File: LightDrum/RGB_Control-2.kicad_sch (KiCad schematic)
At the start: 25 parts, among them Q401 PMXB43UNEZ, Q402 PMXB43UNEZ, Q403 PMXB43UNEZ, Q404 PMXB43UNEZ, Q405 PMXB43UNEZ, Q406 PMXB43UNEZ, Q407 PMXB43UNEZ, Q408 PMXB43UNEZ, U401 PCA9634_TSSOP20

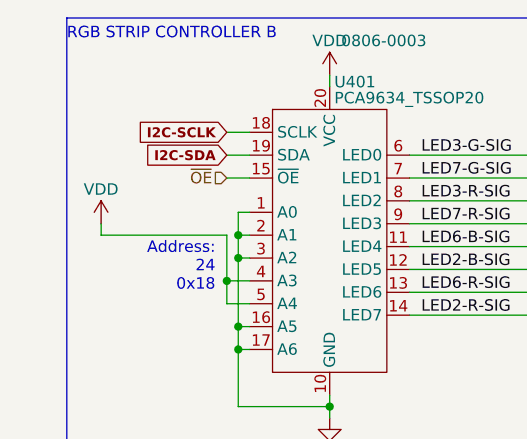
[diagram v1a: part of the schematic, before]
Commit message: Preliminary schematic lock - Starting PCB layout
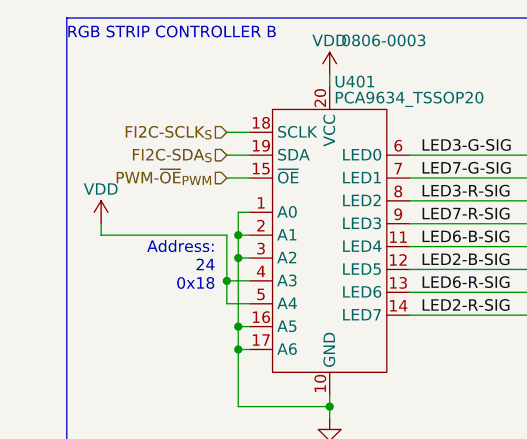
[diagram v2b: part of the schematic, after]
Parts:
- Q401, Q402, Q403, Q404, Q405, Q406, Q407, Q408: SupplierPN (none) -> 1727-PMXB43UNEZCT-ND
- R401, R402, R403, R404, R409, R410, R411, R412: SupplierPN (none) -> RMCF0402FT100RCT-ND
- R405, R406, R407, R408, R413, R414, R415, R416: SupplierPN (none) -> 311-10KJRCT-ND
- U401: SupplierPN (none) -> 568-4066-1-ND
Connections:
- net I2C-SCLK renamed FI2C-SCLK_{S}
- net I2C-SDA renamed FI2C-SDA_{S}
- net ~{OE} renamed PWM-~{OE}_{PWM}
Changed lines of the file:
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@@
   (title_block
     (title "LightDrum")
-    (rev "REV10")
+    (rev "REV11")
     (company "Daxxn Industries")
   )
@@
     (effects (font (size 1.27 1.27)) (justify left bottom))
   )
-  (global_label "I2C-SCLK" (shape input) (at 34.29 29.21 180) (fields_autoplaced)
-    (effects (font (size 1.1 1.1) (thickness 0.254) bold) (justify right))
-    (property "Intersheetrefs" "${INTERSHEET_REFS}" (at 23.7956 29.083 0)
-      (effects (font (size 1.1 1.1) (thickness 0.254) bold) (justify right) hide)
-    )
-  )
-  (global_label "I2C-SDA" (shape input) (at 34.29 31.75 180) (fields_autoplaced)
-    (effects (font (size 1.1 1.1) (thickness 0.254) bold) (justify right))
-    (property "Intersheetrefs" "${INTERSHEET_REFS}" (at 24.8432 31.623 0)
-      (effects (font (size 1.1 1.1) (thickness 0.254) bold) (justify right) hide)
-    )
-  )
   (hierarchical_label "LED6-B" (shape output) (at 102.87 44.45 0) (fields_autoplaced)
     (effects (font (size 1.27 1.27)) (justify left))
   )
-  (hierarchical_label "~{OE}" (shape input) (at 34.29 34.29 180) (fields_autoplaced)
+  (hierarchical_label "FI2C-SCLK_{S}" (shape input) (at 34.29 29.21 180) (fields_autoplaced)
+    (effects (font (size 1.27 1.27)) (justify right))
+  )
+  (hierarchical_label "PWM-~{OE}_{PWM}" (shape input) (at 34.29 34.29 180) (fields_autoplaced)
     (effects (font (size 1.27 1.27)) (justify right))
   )
@@
   (hierarchical_label "LED7-R" (shape output) (at 115.57 68.58 0) (fields_autoplaced)
     (effects (font (size 1.27 1.27)) (justify left))
+  )
+  (hierarchical_label "FI2C-SDA_{S}" (shape input) (at 34.29 31.75 180) (fields_autoplaced)
+    (effects (font (size 1.27 1.27)) (justify right))
   )
   (hierarchical_label "LED7-G" (shape output) (at 166.37 68.58 0) (fields_autoplaced)
@@
       (effects (font (size 1.27 1.27)) hide)
     )
+    (property "SupplierPN" "311-10KJRCT-ND" (at 172.72 53.34 0)
+      (effects (font (size 1.27 1.27)) hide)
+    )
     (pin "1")
     (pin "2")
@@
       (effects (font (size 1.27 1.27)) (justify left))
     )
+    (property "SupplierPN" "1727-PMXB43UNEZCT-ND" (at 163.83 73.66 0)
+      (effects (font (size 1.27 1.27)) hide)
+    )
     (pin "1")
     (pin "2")
@@
     (property "PartNumber" "0806-0003" (at 46.99 19.05 0)
       (effects (font (size 1.27 1.27)) (justify left))
+    )
+    (property "SupplierPN" "568-4066-1-ND" (at 45.72 40.64 0)
+      (effects (font (size 1.27 1.27)) hide)
     )
     (pin "1")
@@
       (effects (font (size 1.27 1.27)) hide)
     )
+    (property "SupplierPN" "311-10KJRCT-ND" (at 185.42 77.47 0)
+      (effects (font (size 1.27 1.27)) hide)
+    )
     (pin "1")
     (pin "2")
@@
       (effects (font (size 1.27 1.27)) hide)
     )
+    (property "SupplierPN" "RMCF0402FT100RCT-ND" (at 172.72 45.72 0)
+      (effects (font (size 1.27 1.27)) hide)
+    )
     (pin "1")
     (pin "2")
@@
       (effects (font (size 1.27 1.27)) hide)
     )
+    (property "SupplierPN" "RMCF0402FT100RCT-ND" (at 160.02 69.85 0)
+      (effects (font (size 1.27 1.27)) hide)
+    )
     (pin "1")
     (pin "2")
@@
       (effects (font (size 1.27 1.27)) hide)
     )
+    (property "SupplierPN" "311-10KJRCT-ND" (at 109.22 77.47 0)
+      (effects (font (size 1.27 1.27)) hide)
+    )
     (pin "1")
     (pin "2")
@@
       (effects (font (size 1.27 1.27)) (justify left))
     )
+    (property "SupplierPN" "1727-PMXB43UNEZCT-ND" (at 100.33 49.53 0)
+      (effects (font (size 1.27 1.27)) hide)
+    )
     (pin "1")
     (pin "2")
@@
       (effects (font (size 1.27 1.27)) (justify left))
     )
+    (property "SupplierPN" "1727-PMXB43UNEZCT-ND" (at 151.13 49.53 0)
+      (effects (font (size 1.27 1.27)) hide)
+    )
     (pin "1")
     (pin "2")
@@
       (effects (font (size 1.27 1.27)) hide)
     )
+    (property "SupplierPN" "RMCF0402FT100RCT-ND" (at 147.32 45.72 0)
+      (effects (font (size 1.27 1.27)) hide)
+    )
     (pin "1")
     (pin "2")
@@
       (effects (font (size 1.27 1.27)) hide)
     )
+    (property "SupplierPN" "RMCF0402FT100RCT-ND" (at 134.62 69.85 0)
+      (effects (font (size 1.27 1.27)) hide)
+    )
     (pin "1")
     (pin "2")
@@
       (effects (font (size 1.27 1.27)) (justify left))
     )
+    (property "SupplierPN" "1727-PMXB43UNEZCT-ND" (at 113.03 73.66 0)
+      (effects (font (size 1.27 1.27)) hide)
+    )
     (pin "1")
     (pin "2")
@@
     (property "PartNumber" "0703-0003" (at 128.27 45.72 0)
       (effects (font (size 1.27 1.27)) (justify left))
+    )
+    (property "SupplierPN" "1727-PMXB43UNEZCT-ND" (at 125.73 49.53 0)
+      (effects (font (size 1.27 1.27)) hide)
     )
     (pin "1")
@@
       (effects (font (size 1.27 1.27)) hide)
     )
+    (property "SupplierPN" "RMCF0402FT100RCT-ND" (at 121.92 45.72 0)
+      (effects (font (size 1.27 1.27)) hide)
+    )
     (pin "1")
     (pin "2")
@@
       (effects (font (size 1.27 1.27)) hide)
     )
+    (property "SupplierPN" "311-10KJRCT-ND" (at 147.32 53.34 0)
+      (effects (font (size 1.27 1.27)) hide)
+    )
     (pin "1")
     (pin "2")
@@
       (effects (font (size 1.27 1.27)) hide)
     )
+    (property "SupplierPN" "311-10KJRCT-ND" (at 134.62 77.47 0)
+      (effects (font (size 1.27 1.27)) hide)
+    )
     (pin "1")
     (pin "2")
@@
       (effects (font (size 1.27 1.27)) hide)
     )
+    (property "SupplierPN" "RMCF0402FT100RCT-ND" (at 96.52 45.72 0)
+      (effects (font (size 1.27 1.27)) hide)
+    )
     (pin "1")
     (pin "2")
@@
       (effects (font (size 1.27 1.27)) hide)
     )
+    (property "SupplierPN" "RMCF0402FT100RCT-ND" (at 109.22 69.85 0)
+      (effects (font (size 1.27 1.27)) hide)
+    )
     (pin "1")
     (pin "2")
@@
       (effects (font (size 1.27 1.27)) hide)
     )
+    (property "SupplierPN" "311-10KJRCT-ND" (at 160.02 77.47 0)
+      (effects (font (size 1.27 1.27)) hide)
+    )
     (pin "1")
     (pin "2")
@@
       (effects (font (size 1.27 1.27)) (justify left))
     )
+    (property "SupplierPN" "1727-PMXB43UNEZCT-ND" (at 138.43 73.66 0)
+      (effects (font (size 1.27 1.27)) hide)
+    )
     (pin "1")
     (pin "2")
@@
       (effects (font (size 1.27 1.27)) hide)
     )
+    (property "SupplierPN" "311-10KJRCT-ND" (at 121.92 53.34 0)
+      (effects (font (size 1.27 1.27)) hide)
+    )
     (pin "1")
     (pin "2")
@@
       (effects (font (size 1.27 1.27)) hide)
     )
+    (property "SupplierPN" "RMCF0402FT100RCT-ND" (at 185.42 69.85 0)
+      (effects (font (size 1.27 1.27)) hide)
+    )
     (pin "1")
     (pin "2")
@@
       (effects (font (size 1.27 1.27)) (justify left))
     )
+    (property "SupplierPN" "1727-PMXB43UNEZCT-ND" (at 176.53 49.53 0)
+      (effects (font (size 1.27 1.27)) hide)
+    )
     (pin "1")
     (pin "2")
@@
       (effects (font (size 1.27 1.27)) (justify left))
     )
+    (property "SupplierPN" "1727-PMXB43UNEZCT-ND" (at 189.23 73.66 0)
+      (effects (font (size 1.27 1.27)) hide)
+    )
     (pin "1")
     (pin "2")
@@
       (effects (font (size 1.27 1.27)) hide)
     )
+    (property "SupplierPN" "311-10KJRCT-ND" (at 96.52 53.34 0)
+      (effects (font (size 1.27 1.27)) hide)
+    )

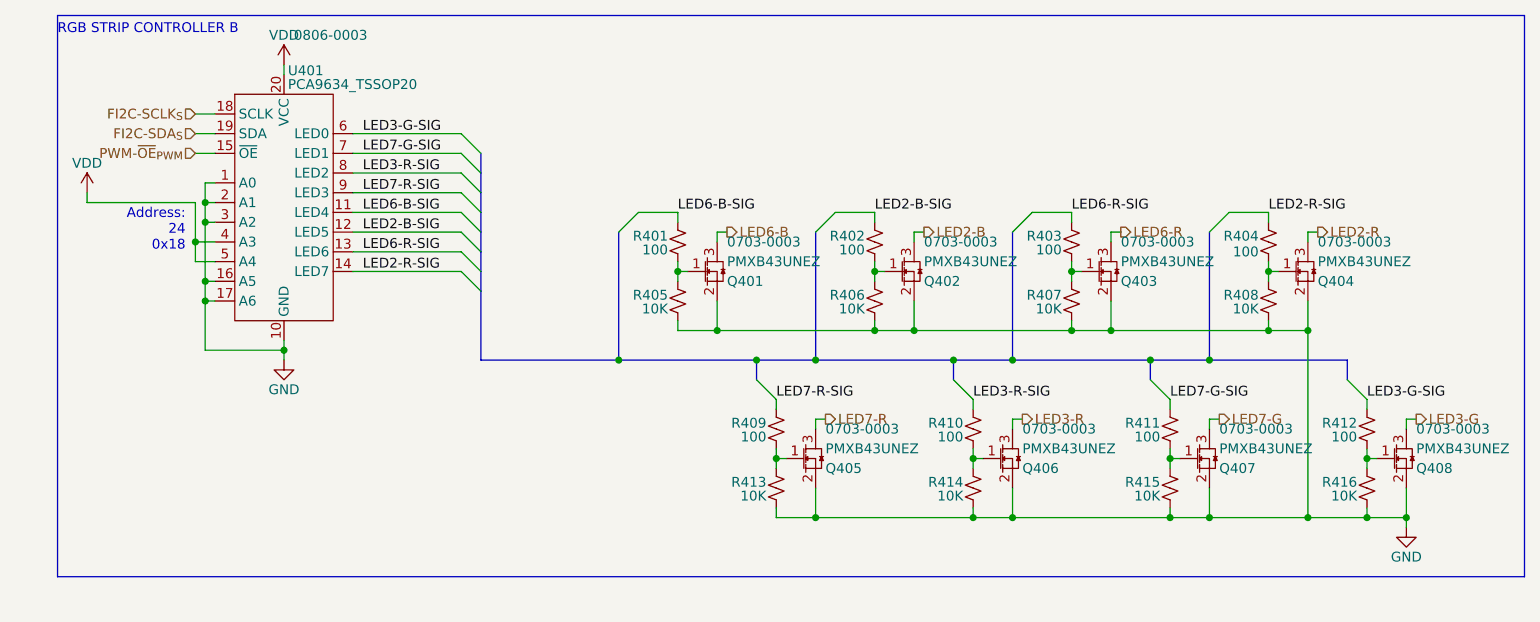
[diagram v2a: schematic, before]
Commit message: Component placement complete
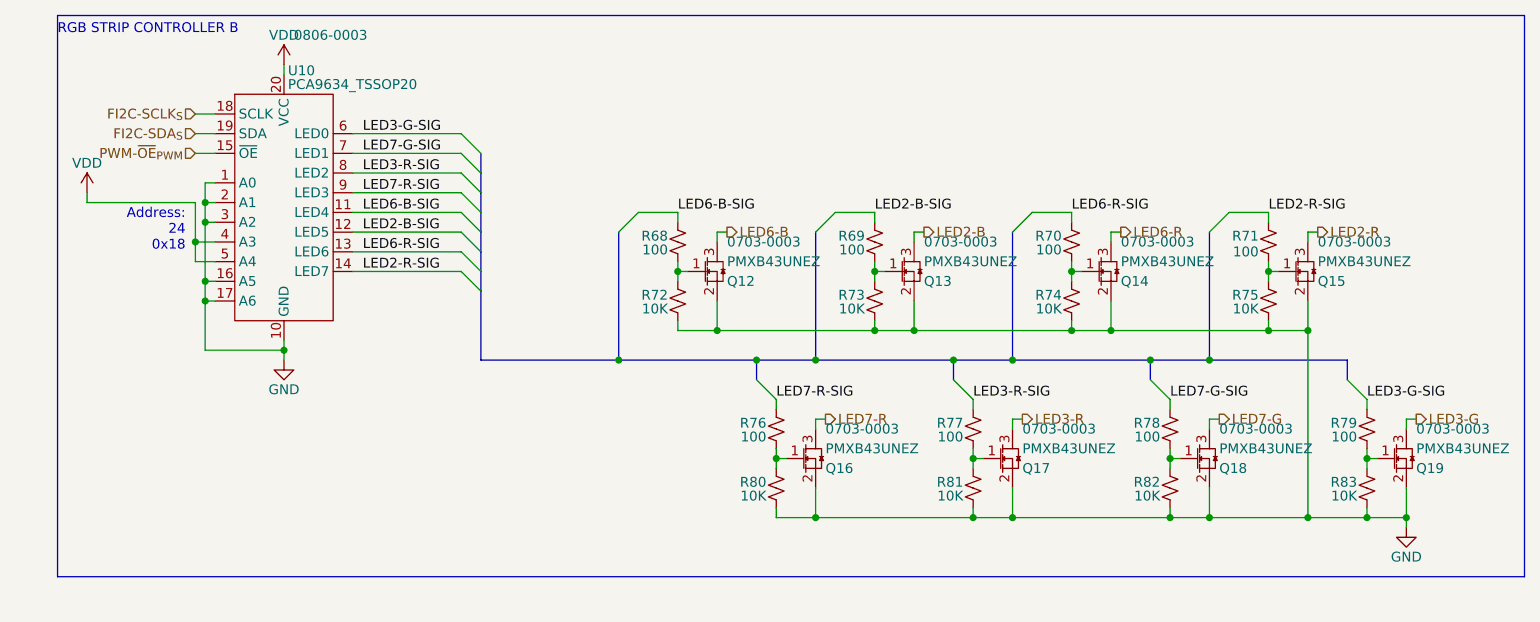
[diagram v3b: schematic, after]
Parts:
- renumbered Q401 to Q12, Q402 to Q13, Q403 to Q14, Q404 to Q15, Q405 to Q16, Q406 to Q17, Q407 to Q18, Q408 to Q19, R401 to R68, R402 to R69, R403 to R70, R404 to R71, R405 to R72, R406 to R73, R407 to R74, R408 to R75, R409 to R76, R410 to R77, R411 to R78, R412 to R79, R413 to R80, R414 to R81, R415 to R82, R416 to R83, U401 to U10

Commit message: First draft layout almost complete
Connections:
- net LED3-G-SIG: now also U10.9 (LED3); no longer U10.6 (LED0)
- net LED3-R-SIG: now also U10.7 (LED1); no longer U10.8 (LED2)
- net LED7-G-SIG: now also U10.8 (LED2); no longer U10.7 (LED1)
- net LED7-R-SIG: now also U10.6 (LED0); no longer U10.9 (LED3)
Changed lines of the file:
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@@
     (effects (font (size 1.27 1.27)) (justify left bottom))
   )
-  (label "LED7-R-SIG" (at 55.88 39.37 0) (fields_autoplaced)
+  (label "LED7-R-SIG" (at 55.88 31.75 0) (fields_autoplaced)
     (effects (font (size 1.27 1.27)) (justify left bottom))
   )
@@
     (effects (font (size 1.27 1.27)) (justify left bottom))
   )
-  (label "LED3-G-SIG" (at 55.88 31.75 0) (fields_autoplaced)
+  (label "LED3-G-SIG" (at 55.88 39.37 0) (fields_autoplaced)
     (effects (font (size 1.27 1.27)) (justify left bottom))
   )
@@
     (effects (font (size 1.27 1.27)) (justify left bottom))
   )
-  (label "LED7-G-SIG" (at 55.88 34.29 0) (fields_autoplaced)
+  (label "LED7-G-SIG" (at 55.88 36.83 0) (fields_autoplaced)
     (effects (font (size 1.27 1.27)) (justify left bottom))
   )
@@
     (effects (font (size 1.27 1.27)) (justify left bottom))
   )
-  (label "LED3-R-SIG" (at 55.88 36.83 0) (fields_autoplaced)
+  (label "LED3-R-SIG" (at 55.88 34.29 0) (fields_autoplaced)
     (effects (font (size 1.27 1.27)) (justify left bottom))
   )

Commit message: Minor fixes and cleanup - REV11
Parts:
- added C75, C76: 100nF, Capacitor_SMD:C_0402_1005Metric, symbol Daxxn_Device:C
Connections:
- net GND: now also C75.2, C76.2
- net VDD: now also C75.1, C76.1
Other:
- moved on the sheet: Q12, Q13, Q14, Q15, Q16, Q17, Q18, Q19, R68, R69, R70, R71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

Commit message: Replace DSub with much better ECU conn
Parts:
- removed C75, C76: 100nF, Capacitor_SMD:C_0402_1005Metric, symbol Daxxn_Device:C
- removed Q12, Q13, Q14, Q15, Q16, Q17, Q18, Q19: PMXB43UNEZ, Daxxn_Packages:DFN1010D-3, symbol Daxxn_Transistors:PMXB43UNEZ
- removed R68, R69, R70, R71, R76, R77, R78, R79: 100, Resistor_SMD:R_0402_1005Metric, symbol Device:R_Small_US
- removed R72, R73, R74, R75, R80, R81, R82, R83: 10K, Resistor_SMD:R_0402_1005Metric, symbol Device:R_Small_US
- removed U10: PCA9634_TSSOP20, Package_SO:TSSOP-20_4.4x6.5mm_P0.65mm, symbol Daxxn_IC:PCA9634_TSSOP20
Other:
- note removed: "Address: 24 0x18"
- note removed: "RGB STRIP CONTROLLER B"
